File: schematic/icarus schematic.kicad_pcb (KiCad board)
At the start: 2 copper layers, 2 parts, among them U1 ESP32-S3, U2 BMI088

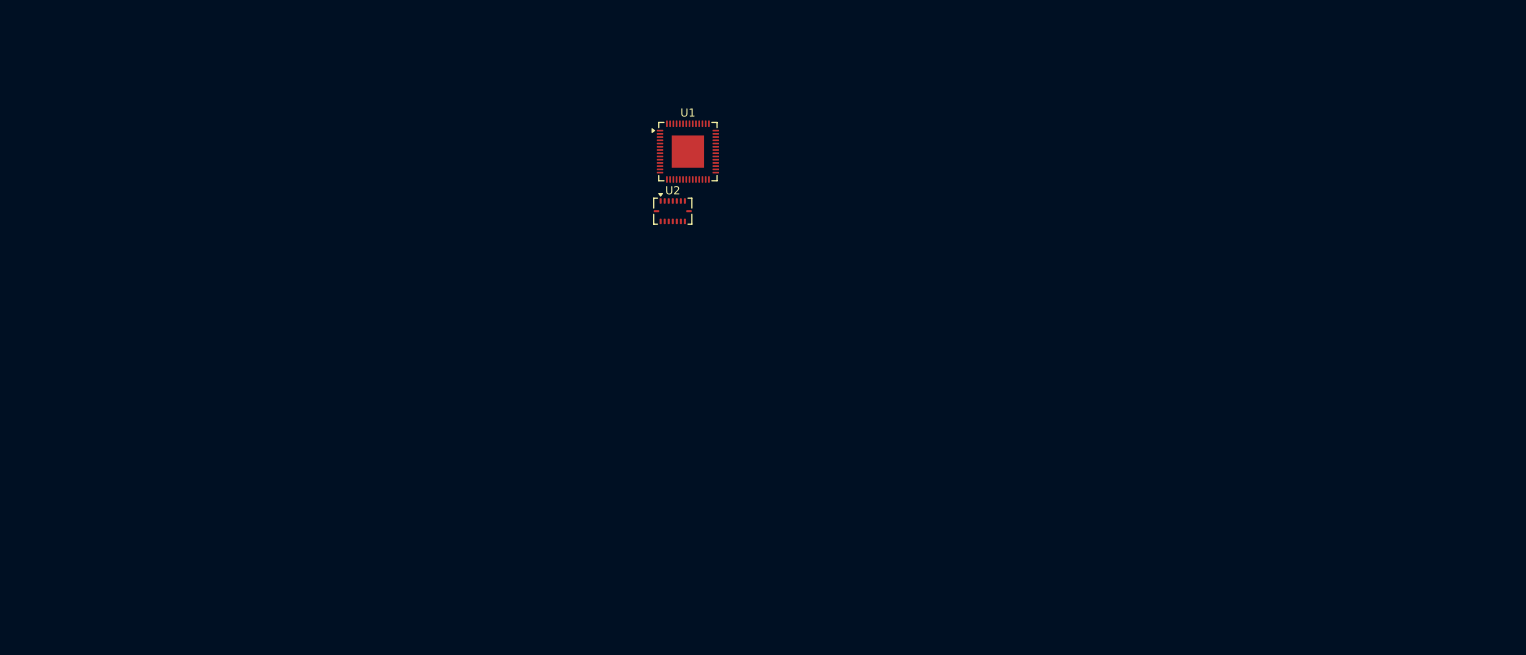
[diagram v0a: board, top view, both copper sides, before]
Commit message: Added connectors instead of motors.
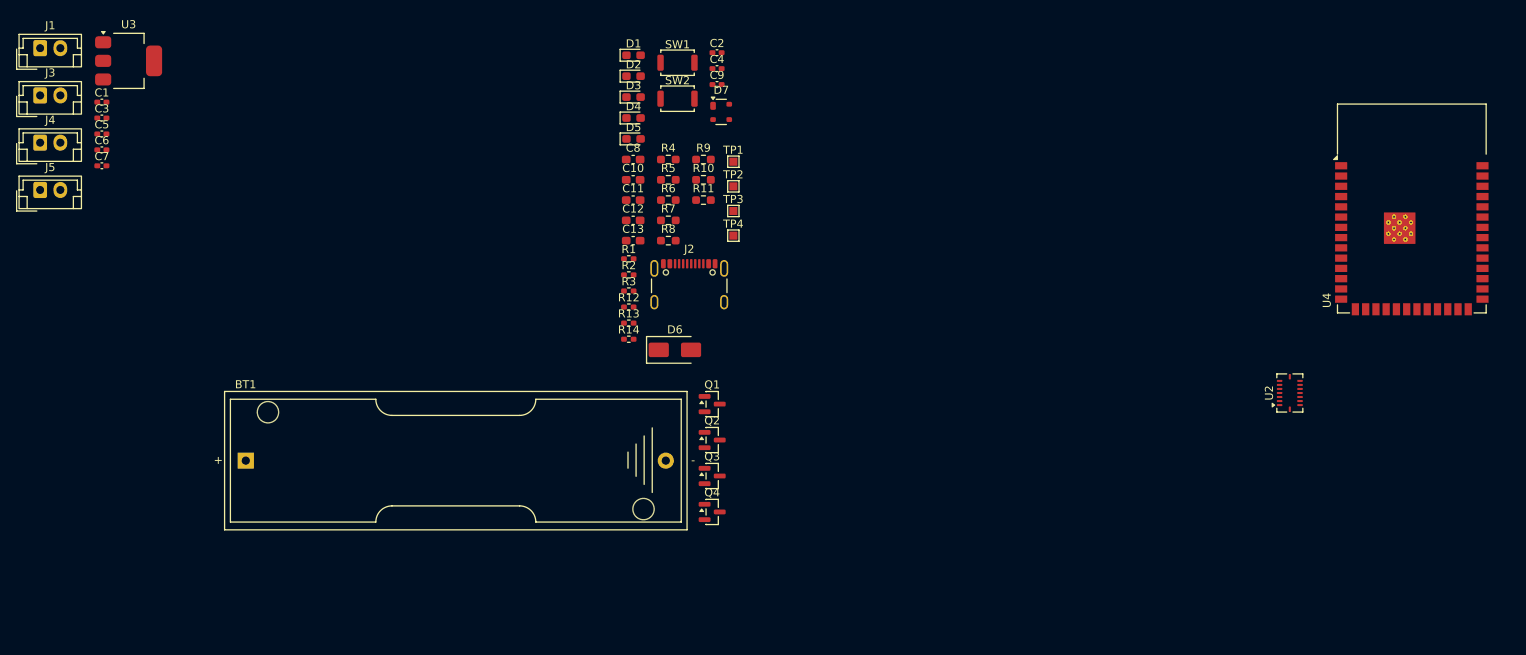
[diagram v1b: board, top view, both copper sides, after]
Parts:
- removed U1: ESP32-S3, Package_DFN_QFN:QFN-56-1EP_7x7mm_P0.4mm_EP4x4mm
- added BT1: 5V, Battery:BatteryHolder_Keystone_2460_1xAA, F.Cu at (68.8, 109.4)
- added C1: 10uF, Capacitor_SMD:C_0402_1005Metric_Pad0.74x0.62mm_HandSolder, F.Cu at (51.0, 65.0)
- added C10: 0.1uF, Capacitor_SMD:C_0603_1608Metric_Pad1.08x0.95mm_HandSolder, F.Cu at (116.7, 74.6)
- added C11: 0.1uF, Capacitor_SMD:C_0603_1608Metric_Pad1.08x0.95mm_HandSolder, F.Cu at (116.7, 77.1)
- added C12: 0.1uF, Capacitor_SMD:C_0603_1608Metric_Pad1.08x0.95mm_HandSolder, F.Cu at (116.7, 79.6)
- added C13: 0.1uF, Capacitor_SMD:C_0603_1608Metric_Pad1.08x0.95mm_HandSolder, F.Cu at (116.7, 82.1)
- added C2: 0.1uF, Capacitor_SMD:C_0402_1005Metric_Pad0.74x0.62mm_HandSolder, F.Cu at (127.1, 58.9)
- added C3: 10uF, Capacitor_SMD:C_0402_1005Metric_Pad0.74x0.62mm_HandSolder, F.Cu at (51.0, 67.0)
- added C4: 0.1uF, Capacitor_SMD:C_0402_1005Metric_Pad0.74x0.62mm_HandSolder, F.Cu at (127.1, 60.9)
- added C5: 100nf, Capacitor_SMD:C_0402_1005Metric_Pad0.74x0.62mm_HandSolder, F.Cu at (51.0, 68.9)
- added C6: 100nf, Capacitor_SMD:C_0402_1005Metric_Pad0.74x0.62mm_HandSolder, F.Cu at (51.0, 70.9)
- added C7: 100nf, Capacitor_SMD:C_0402_1005Metric_Pad0.74x0.62mm_HandSolder, F.Cu at (51.0, 72.9)
- added C8: 470uF, Capacitor_SMD:C_0603_1608Metric_Pad1.08x0.95mm_HandSolder, F.Cu at (116.7, 72.1)
- added C9: 100nf, Capacitor_SMD:C_0402_1005Metric_Pad0.74x0.62mm_HandSolder, F.Cu at (127.1, 62.8)
- added D1: LED, LED_SMD:LED_0603_1608Metric_Pad1.05x0.95mm_HandSolder, F.Cu at (116.8, 59.2)
- added D2: 1N5819, Diode_SMD:D_0603_1608Metric_Pad1.05x0.95mm_HandSolder, F.Cu at (116.8, 61.8)
- added D3: 1N5819, Diode_SMD:D_0603_1608Metric_Pad1.05x0.95mm_HandSolder, F.Cu at (116.8, 64.4)
- added D4: 1N5819, Diode_SMD:D_0603_1608Metric_Pad1.05x0.95mm_HandSolder, F.Cu at (116.8, 67.0)
- added D5: 1N5819, Diode_SMD:D_0603_1608Metric_Pad1.05x0.95mm_HandSolder, F.Cu at (116.8, 69.6)
- added D6: SS14, Diode_SMD:D_SMA, F.Cu at (121.9, 95.7)
- added D7: SP0503BAHT, Package_TO_SOT_SMD:SOT-143, F.Cu at (127.6, 66.2)
- added J1: Conn_01x02_Socket, Connector_JST:JST_EH_B2B-EH-A_1x02_P2.50mm_Vertical, F.Cu at (43.3, 58.3)
- added J2: USB_C_Receptacle_USB2.0_16P, Connector_USB:USB_C_Receptacle_GCT_USB4105-xx-A_16P_TopMnt_Horizontal, F.Cu at (123.7, 88.7)
- added J3: Conn_01x02_Socket, Connector_JST:JST_EH_B2B-EH-A_1x02_P2.50mm_Vertical, F.Cu at (43.3, 64.2)
- added J4: Conn_01x02_Socket, Connector_JST:JST_EH_B2B-EH-A_1x02_P2.50mm_Vertical, F.Cu at (43.3, 70.0)
- added J5: Conn_01x02_Socket, Connector_JST:JST_EH_B2B-EH-A_1x02_P2.50mm_Vertical, F.Cu at (43.3, 75.9)
- added Q1: AO3400A, Package_TO_SOT_SMD:SOT-23, F.Cu at (126.5, 102.4)
- added Q2: AO3400A, Package_TO_SOT_SMD:SOT-23, F.Cu at (126.5, 106.8)
- added Q3: AO3400A, Package_TO_SOT_SMD:SOT-23, F.Cu at (126.5, 111.3)
- added Q4: AO3400A, Package_TO_SOT_SMD:SOT-23, F.Cu at (126.5, 115.7)
- added R1: 220ohm, Resistor_SMD:R_0402_1005Metric_Pad0.72x0.64mm_HandSolder, F.Cu at (116.2, 84.4)
- added R10: 10k, Resistor_SMD:R_0603_1608Metric_Pad0.98x0.95mm_HandSolder, F.Cu at (125.4, 74.6)
- added R11: 10k, Resistor_SMD:R_0603_1608Metric_Pad0.98x0.95mm_HandSolder, F.Cu at (125.4, 77.1)
- added R12: 10k, Resistor_SMD:R_0402_1005Metric_Pad0.72x0.64mm_HandSolder, F.Cu at (116.2, 90.4)
- added R13: 5.1k, Resistor_SMD:R_0402_1005Metric_Pad0.72x0.64mm_HandSolder, F.Cu at (116.2, 92.4)
- added R14: 5.1k, Resistor_SMD:R_0402_1005Metric_Pad0.72x0.64mm_HandSolder, F.Cu at (116.2, 94.3)
- added R2: 10k, Resistor_SMD:R_0402_1005Metric_Pad0.72x0.64mm_HandSolder, F.Cu at (116.2, 86.4)
- added R3: 10k, Resistor_SMD:R_0402_1005Metric_Pad0.72x0.64mm_HandSolder, F.Cu at (116.2, 88.4)
- added R4: 100, Resistor_SMD:R_0603_1608Metric_Pad0.98x0.95mm_HandSolder, F.Cu at (121.1, 72.1)
- added R5: 100, Resistor_SMD:R_0603_1608Metric_Pad0.98x0.95mm_HandSolder, F.Cu at (121.1, 74.6)
- added R6: 100, Resistor_SMD:R_0603_1608Metric_Pad0.98x0.95mm_HandSolder, F.Cu at (121.1, 77.1)
- added R7: 100, Resistor_SMD:R_0603_1608Metric_Pad0.98x0.95mm_HandSolder, F.Cu at (121.1, 79.6)
- added R8: 10k, Resistor_SMD:R_0603_1608Metric_Pad0.98x0.95mm_HandSolder, F.Cu at (121.1, 82.1)
- added R9: 10k, Resistor_SMD:R_0603_1608Metric_Pad0.98x0.95mm_HandSolder, F.Cu at (125.4, 72.1)
- added SW1: SW_Push(BOOt), Button_Switch_SMD:SW_Push_SPST_NO_Alps_SKRK, F.Cu at (122.2, 60.1)
- added SW2: SW_Push(EN), Button_Switch_SMD:SW_Push_SPST_NO_Alps_SKRK, F.Cu at (122.2, 64.6)
- added TP1: TestPoint, TestPoint:TestPoint_Pad_1.0x1.0mm, F.Cu at (129.1, 72.4)
- added TP2: TestPoint, TestPoint:TestPoint_Pad_1.0x1.0mm, F.Cu at (129.1, 75.4)
- added TP3: TestPoint, TestPoint:TestPoint_Pad_1.0x1.0mm, F.Cu at (129.1, 78.5)
- added TP4: TestPoint, TestPoint:TestPoint_Pad_1.0x1.0mm, F.Cu at (129.1, 81.5)
- added U3: AMS1117-3.3, Package_TO_SOT_SMD:SOT-223-3_TabPin2, F.Cu at (54.3, 59.9)
- added U4: ESP32-S3-WROOM-1, RF_Module:ESP32-S3-WROOM-1, F.Cu at (213.1, 78.1)
- moved U2 79.6 mm to (198.0, 101.0), turned to 90 degrees
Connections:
- U2 pad 10: unconnected-(U2-SDO2-Pad10) -> /SD02
- U2 pad 11: unconnected-(U2-VDDIO-Pad11) -> /3.3V
- U2 pad 12: unconnected-(U2-INT3-Pad12) -> /INT3
- U2 pad 14: unconnected-(U2-~{CSB1}-Pad14) -> /CSB1
- U2 pad 15: unconnected-(U2-SDO1-Pad15) -> /SD01
- U2 pad 16: unconnected-(U2-INT1-Pad16) -> /INT1
- U2 pad 2: Net-(U2-GNDA-Pad2) -> GND
- U2 pad 3: unconnected-(U2-VDD-Pad3) -> /3.3V
- U2 pad 4: Net-(U2-GNDA-Pad2) -> GND
- U2 pad 5: unconnected-(U2-~{CSB2}-Pad5) -> /CSB2
- U2 pad 6: unconnected-(U2-GNDIO-Pad6) -> GND
- U2 pad 7: unconnected-(U2-PS-Pad7) -> GND
- U2 pad 8: unconnected-(U2-SCK/SCL-Pad8) -> /SCK
- U2 pad 9: unconnected-(U2-SDI/SDA-Pad9) -> /SDI

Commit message: PCB first iteration.
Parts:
- removed BT1: 5V, Battery:BatteryHolder_Keystone_2460_1xAA
- added TP5: TestPoint, TestPoint:TestPoint_Pad_4.0x4.0mm, F.Cu at (220.2, 99.8)
- added TP6: TestPoint, TestPoint:TestPoint_Pad_4.0x4.0mm, F.Cu at (220.2, 105.5)
- moved J1 181.8 mm to (217.5, 110.5)
- moved J3 181.8 mm to (217.5, 116.2)
- moved J5 181.7 mm to (217.5, 127.8)
- moved J4 181.7 mm to (217.5, 121.8)
- moved C6 154.2 mm to (202.2, 101.0), turned to -90 degrees
- moved C1 138.9 mm to (186.4, 96.0)
- moved C7 134.0 mm to (183.0, 96.0)
- moved C5 134.0 mm to (178.8, 109.0), turned to 180 degrees
- moved U3 132.7 mm to (179.8, 103.0), turned to 180 degrees
- moved C3 131.7 mm to (179.4, 96.0)
- moved D5 105.9 mm to (220.1, 92.5)
- moved D4 105.9 mm to (220.4, 88.8)
- moved C11 105.0 mm to (220.1, 95.5), turned to 180 degrees
- moved D3 104.8 mm to (220.1, 82.3)
- moved D2 104.1 mm to (219.9, 76.0)
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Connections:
- C9 pad 1: GND -> (no net)
- C9 pad 2: /EN -> (no net)
- D1 pad 1: GND -> (no net)
- D1 pad 2: Net-(D1-A) -> (no net)
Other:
- board outline added: 50 x 60.2 mm
- board text added: "J2"

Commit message: Schematic change
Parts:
- moved TP3 40.4 mm to (165.0, 97.5)
- moved TP4 40.4 mm to (165.0, 103.8)
- moved C2 39.1 mm to (181.0, 72.8)
- moved C4 39.1 mm to (181.2, 82.2)
- moved C9 39.1 mm to (175.6, 90.5)
- moved R12 39.1 mm to (181.2, 90.5)
- moved R2 39.1 mm to (175.7, 72.8)
- moved R3 39.1 mm to (175.8, 82.2)
- moved SW1 39.1 mm to (178.0, 76.5)
- moved SW2 39.1 mm to (178.0, 85.2)
- moved TP1 25.4 mm to (206.8, 100.2)
- moved TP2 25.4 mm to (206.8, 106.5)
- moved C3 19.6 mm to (181.1, 115.5)
- moved C5 19.6 mm to (180.6, 128.5)
- moved R1 19.6 mm to (177.3, 115.5)
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
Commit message: Merge branch 'main' of https://github.com/Aryan2804/Icarus
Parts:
- C8: footprint Capacitor_SMD:C_0603_1608Metric_Pad1.08x0.95mm_HandSolder -> Capacitor_THT:C_Radial_D6.3mm_H5.0mm_P2.50mm
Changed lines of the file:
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@@
 		)
 	)
-	(footprint "Capacitor_SMD:C_0603_1608Metric_Pad1.08x0.95mm_HandSolder"
+	(footprint "Capacitor_THT:C_Radial_D6.3mm_H5.0mm_P2.50mm"
 		(layer "F.Cu")
 		(at 215.5 104.1375 -90)
-		(descr "Capacitor SMD 0603 (1608 Metric), square (rectangular) end terminal, IPC-7351 nominal with elongated pad for handsoldering. (Body size source: IPC-SM-782 page 76, https://www.pcb-3d.com/wordpress/wp-content/uploads/ipc-sm-782a_amendment_1_and_2.pdf)")
-		(tags "capacitor handsolder")
+		(descr "C, Radial series, Radial, pin pitch=2.50mm, diameter=6.3mm, height=5mm, Non-Polar Electrolytic Capacitor")
+		(tags "C Radial series Radial pin pitch 2.50mm diameter 6.3mm height 5mm Non-Polar Electrolytic Capacitor")
 		(property "Reference" "C8"
-			(at 1.75 -1.6125 90)
+			(at 1.25 -4.4 270)
 			(layer "F.SilkS")
 			(effects
@@
 		)
 		(property "Value" "470uF"
-			(at 0 1.43 90)
+			(at 1.25 4.4 270)
 			(layer "F.Fab")
 			(effects
@@
 		)
 		(property "Datasheet" ""
-			(at 0 0 90)
+			(at 0 0 270)
 			(layer "F.Fab")
 			(hide yes)
@@
 		)
 		(property "Description" "Unpolarized capacitor"
-			(at 0 0 90)
+			(at 0 0 270)
 			(layer "F.Fab")
 			(hide yes)
@@
 			)
 		)
-		(property "KiLib_Generator" "SMD_2terminal_chip_molded"
-			(at 0 0 90)
+		(property "KiLib_Generator" "capacitor/THT/other"
+			(at 0 0 270)
 			(layer "F.SilkS")
 			(hide yes)
@@
 			)
 		)
-		(attr smd)
+		(attr through_hole)
 		(duplicate_pad_numbers_are_jumpers no)
-		(fp_line
-			(start -0.146267 0.51)
-			(end 0.146267 0.51)
+		(fp_circle
+			(center 1.25 0)
+			(end 4.52 0)
 			(stroke
 				(width 0.12)
 				(type solid)
 			)
+			(fill no)
 			(layer "F.SilkS")
 		)
-		(fp_line
-			(start -0.146267 -0.51)
-			(end 0.146267 -0.51)
-			(stroke
-				(width 0.12)
-				(type solid)
-			)
-			(layer "F.SilkS")
-		)
-		(fp_rect
-			(start -1.65 -0.73)
-			(end 1.65 0.73)
+		(fp_circle
+			(center 1.25 0)
+			(end 4.65 0)
 			(stroke
 				(width 0.05)
@@
 			(layer "F.CrtYd")
 		)
-		(fp_rect
-			(start -0.8 -0.4)
-			(end 0.8 0.4)
+		(fp_circle
+			(center 1.25 0)
+			(end 4.4 0)
 			(stroke
 				(width 0.1)
@@
 		)
 		(fp_text user "${REFERENCE}"
-			(at 0 0 90)
+			(at 1.25 0 270)
 			(layer "F.Fab")
 			(effects
 				(font
-					(size 0.4 0.4)
-					(thickness 0.06)
+					(size 1 1)
+					(thickness 0.15)
 				)
 			)
 		)
-		(pad "1" smd roundrect
-			(at -0.8625 0 270)
-			(size 1.075 0.95)
-			(layers "F.Cu" "F.Mask" "F.Paste")
-			(roundrect_rratio 0.25)
+		(pad "1" thru_hole circle
+			(at 0 0 270)
+			(size 1.6 1.6)
+			(drill 0.8)
+			(layers "*.Cu" "*.Mask")
+			(remove_unused_layers no)
 			(net "Net-(D2-K)")
 			(pintype "passive")
 		)
-		(pad "2" smd roundrect
-			(at 0.8625 0 270)
-			(size 1.075 0.95)
-			(layers "F.Cu" "F.Mask" "F.Paste")
-			(roundrect_rratio 0.25)
+		(pad "2" thru_hole circle
+			(at 2.5 0 270)
+			(size 1.6 1.6)
+			(drill 0.8)
+			(layers "*.Cu" "*.Mask")
+			(remove_unused_layers no)
 			(net "GND")
 			(pintype "passive")
 		)
 		(embedded_fonts no)
-		(model "${KICAD10_3DMODEL_DIR}/Capacitor_SMD.3dshapes/C_0603_1608Metric.step"
+		(model "${KICAD10_3DMODEL_DIR}/Capacitor_THT.3dshapes/C_Radial_D6.3mm_H5.0mm_P2.50mm.step"
 			(offset
 				(xyz 0 0 0)
